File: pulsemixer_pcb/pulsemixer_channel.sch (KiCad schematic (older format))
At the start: 21 parts, among them Q201 Q_NPN_BEC, SW501 Vol_Encoder, SW502 SW_PUSH_SPST, U501 MCP23017_SP, U502 74LVC2G17

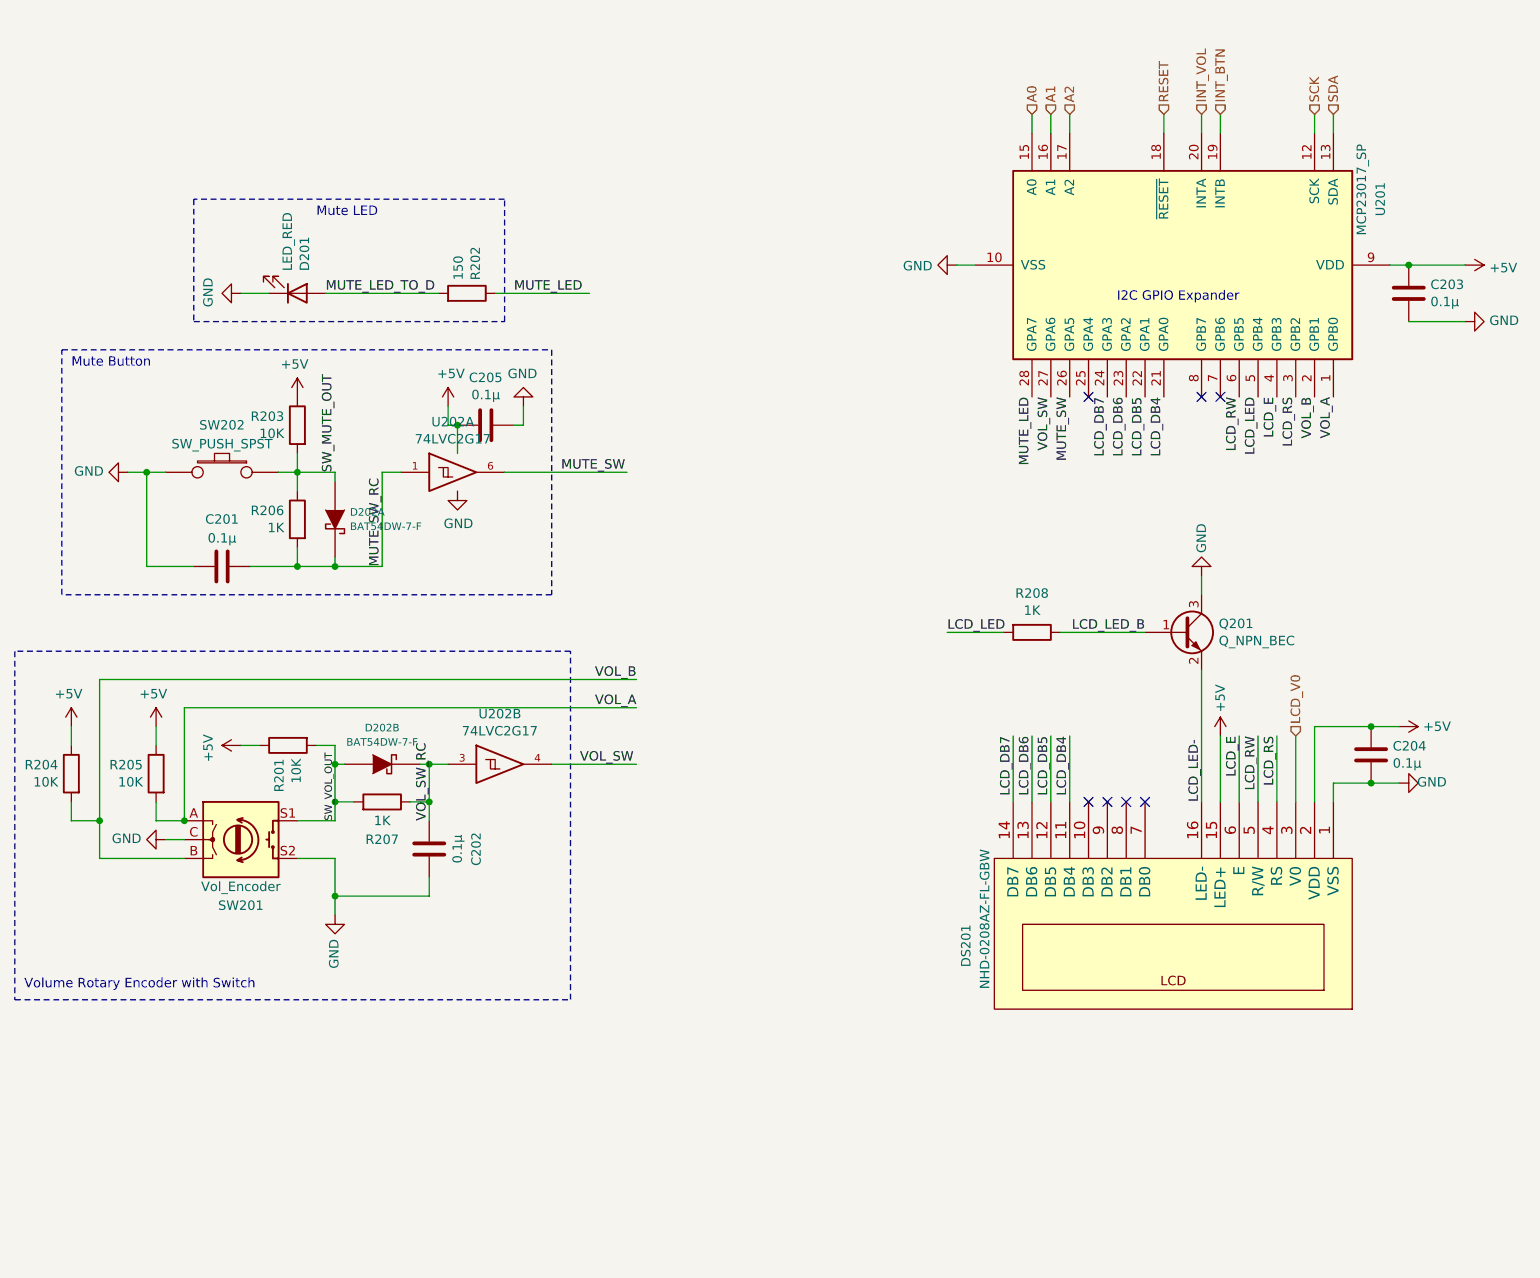
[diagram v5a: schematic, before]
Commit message: Added another AND gate to include master section buttons in the buttn interrupt logic.
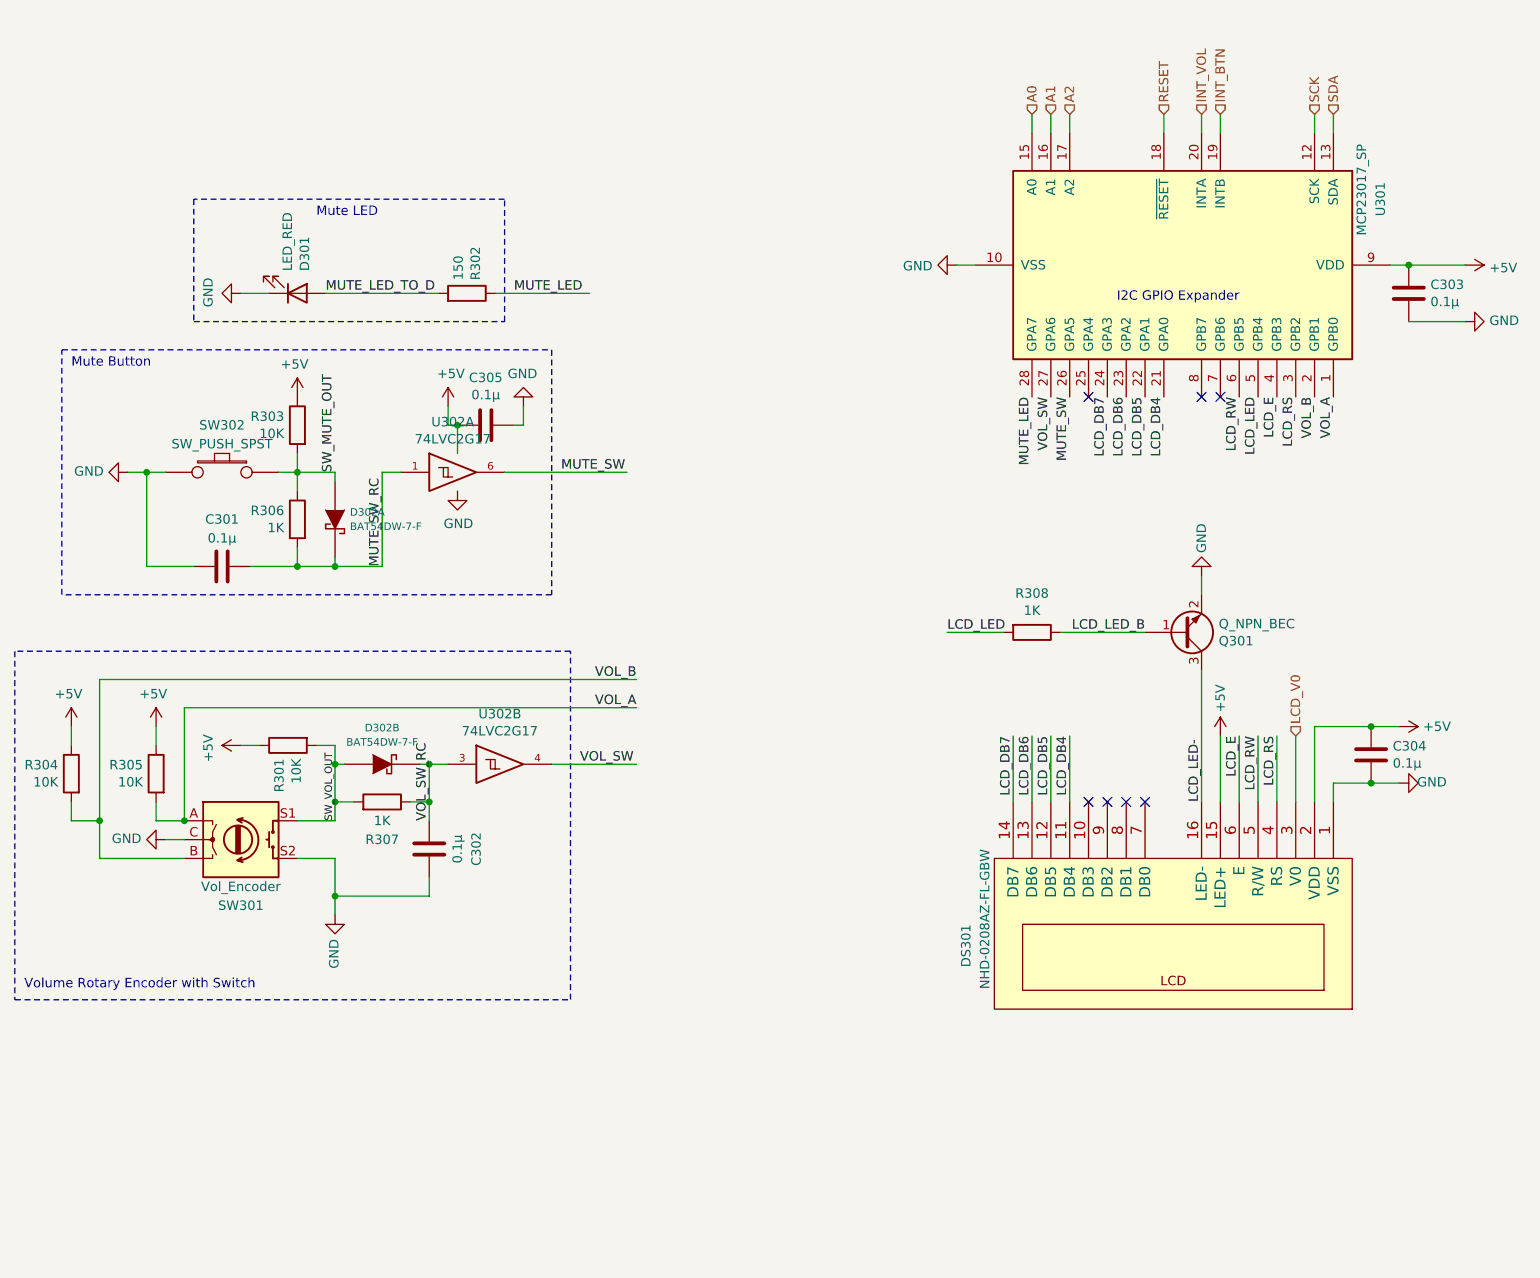
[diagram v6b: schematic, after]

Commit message: Finalized changes to board and sent for fabrication.
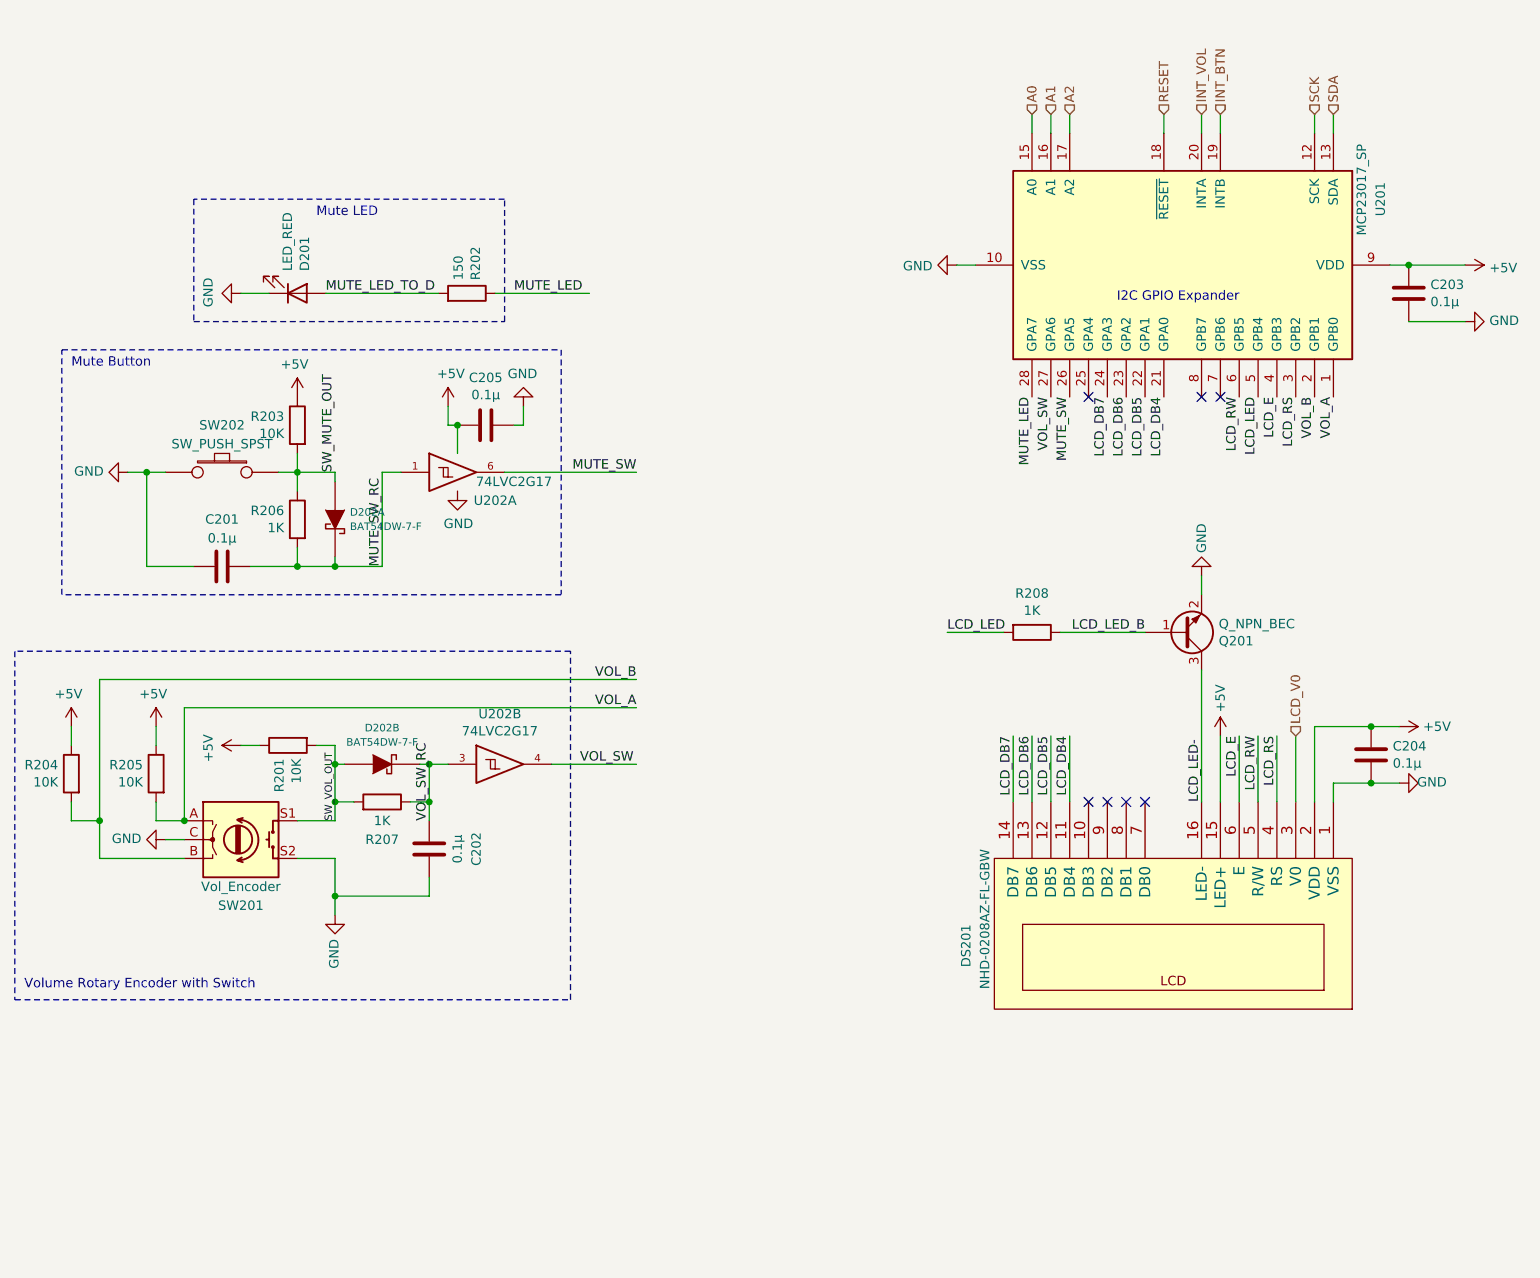
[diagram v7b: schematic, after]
